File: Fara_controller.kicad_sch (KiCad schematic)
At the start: 74 parts, among them U1 XL1509-12, U2 XL1509-05, U3 TPS61165DBV, U4 TPS61165DBV, U6 TPS61165DBV, X1 Conn_01x02, X10 Conn_01x02, X11 Conn_01x02, X12 Conn_01x02, X13 Conn_01x02, X14 Conn_01x02, X18 Objective, X19 Conn_01x02, X2 Conn_01x02, X20 Conn_01x03, X21 Conn_01x03, X3 Conn_01x02, X4 Conn_01x02, X5 Fan_3pin, X6 Fan_3pin, X7 Fan_3pin, X8 Fan_3pin, X9 Conn_01x02

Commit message: v0.2 draft decomposition was made
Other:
- moved on the sheet: C15, C9, L5, R18, R19, R20, R21, R22, R23, R3, R7, R8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

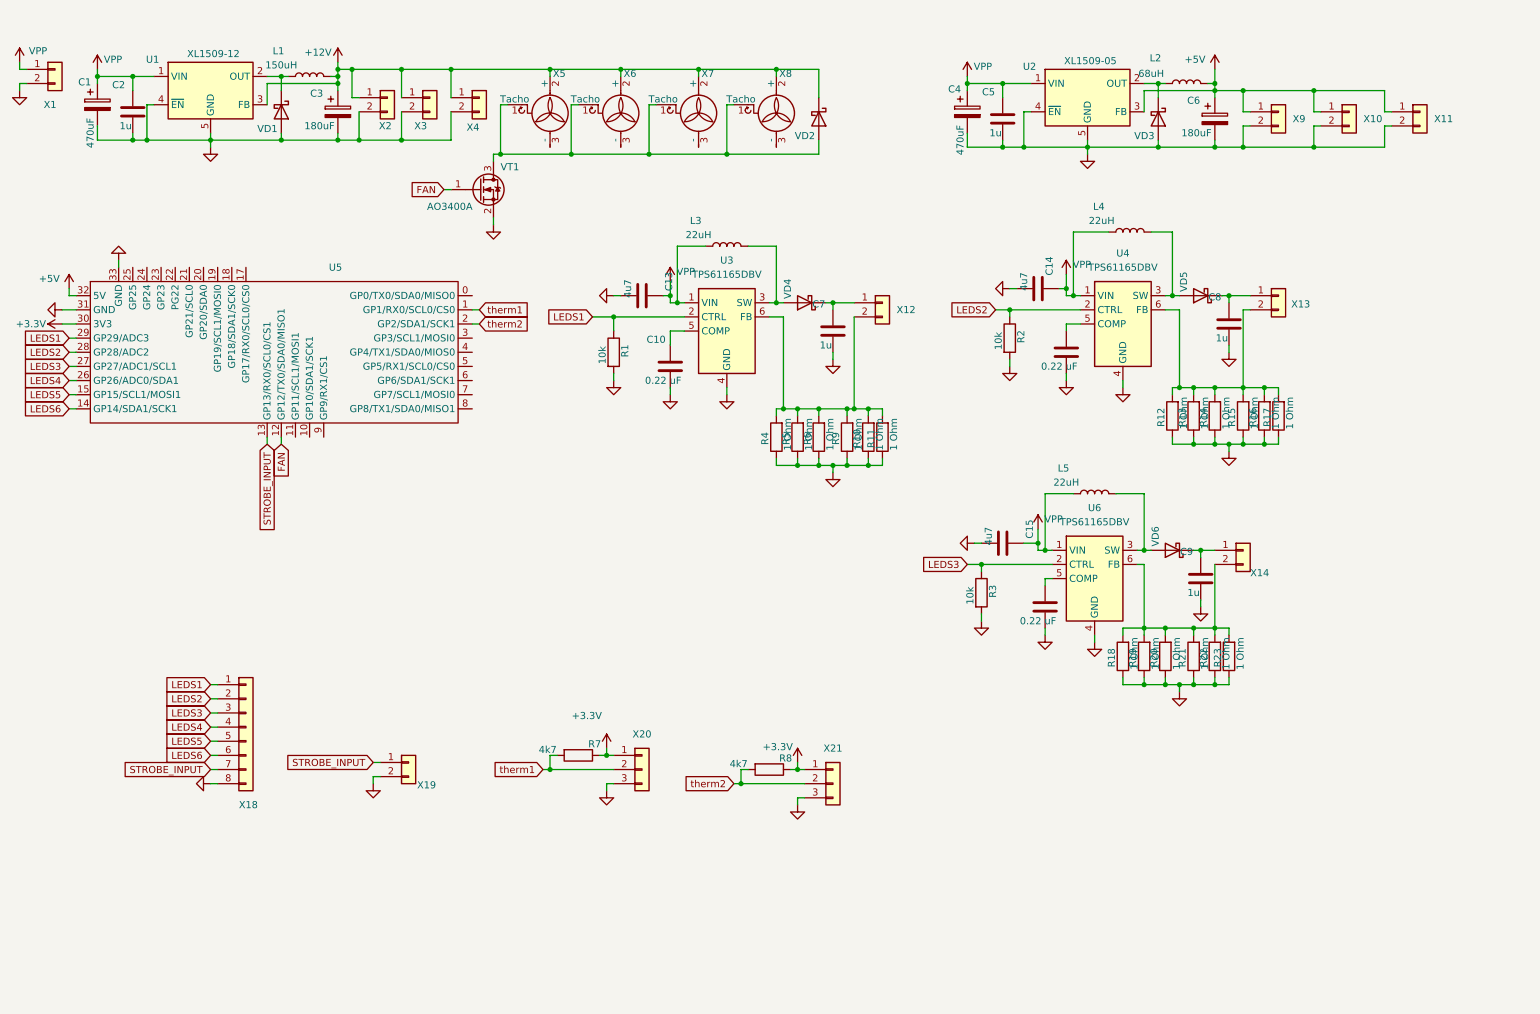
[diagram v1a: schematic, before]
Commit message: v0.3 4th driver was decomposed
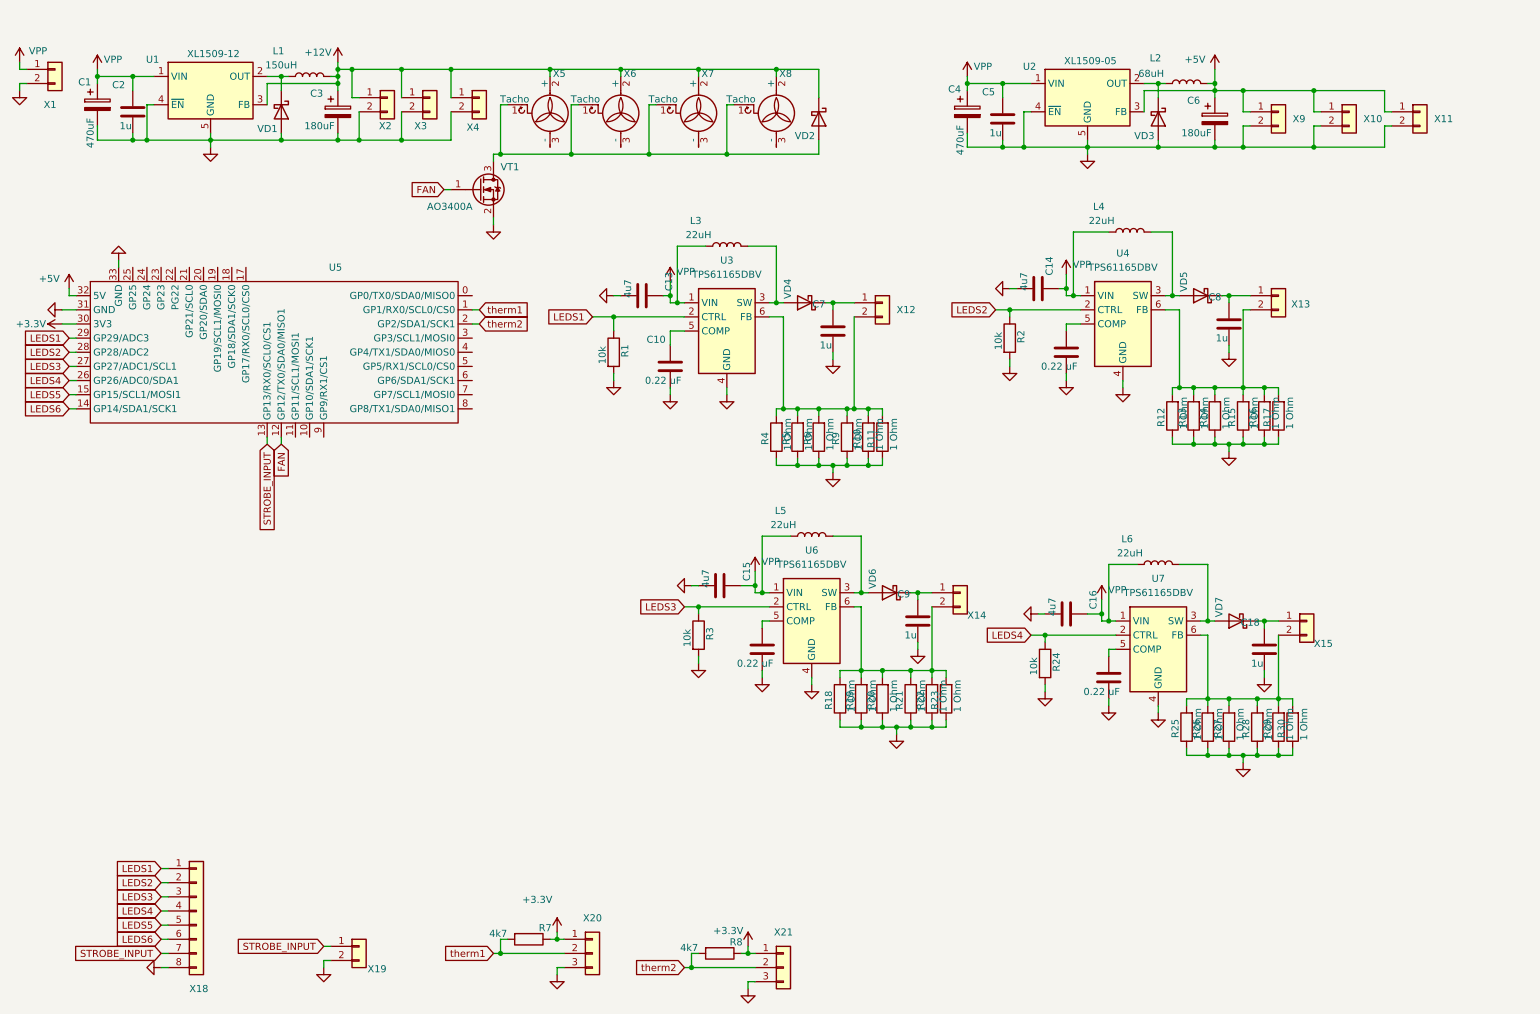
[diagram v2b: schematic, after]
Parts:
- added C16: 4u7, Capacitor_SMD:C_0805_2012Metric_Pad1.18x1.45mm_HandSolder, symbol Device:C
- added C17: 0.22 uF, Capacitor_SMD:C_0603_1608Metric_Pad1.08x0.95mm_HandSolder, symbol Device:C
- added C18: 1u, Capacitor_SMD:C_0603_1608Metric_Pad1.08x0.95mm_HandSolder, symbol Device:C
- added L6: 22uH, Inductor_SMD:L_7.3x7.3_H4.5, symbol Device:L
- added R24: 10k, Resistor_SMD:R_0603_1608Metric_Pad0.98x0.95mm_HandSolder, symbol Device:R
- added R25, R26, R27, R28, R29, R30: 1 Ohm, Resistor_SMD:R_0603_1608Metric_Pad0.98x0.95mm_HandSolder, symbol Device:R
- added U7: TPS61165DBV, Package_TO_SOT_SMD:SOT-23-6, symbol Driver_LED:TPS61165DBV
- added VD7: CDBA3100-HF, Diode_SMD:D_SOD-123, symbol Diode:CDBA3100-HF
- added X15: Conn_01x02, Connector_JST:JST_XH_B2B-XH-A_1x02_P2.50mm_Vertical, symbol Connector_Generic:Conn_01x02
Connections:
- net GND: now also C16.2, C17.2, C18.2, R24.2, R25.1, R26.1, R27.1, R28.1, R29.1, R30.1, U7.4 (GND)
- net LEDS4: now also R24.1, U7.2 (CTRL)
- net VPP: now also C16.1, L6.1, U7.1 (VIN)
- new net: C18.1, VD7.1 (K), X15.1 (Pin_1)
- new net: R25.2, R26.2, R27.2, R28.2, R29.2, R30.2, U7.6 (FB), X15.2 (Pin_2)
- new net: C17.1, U7.5 (COMP)
- new net: L6.2, U7.3 (SW), VD7.2 (A)
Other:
- moved on the sheet: C15, C9, L5, R18, R19, R20, R21, R22, R23, R3, R7, R8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

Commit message: v0.5 actual state
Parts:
- added X16: Conn_01x02, Connector_JST:JST_XH_B2B-XH-A_1x02_P2.50mm_Vertical, symbol Connector_Generic:Conn_01x02
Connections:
- net +12V: now also X16.2 (Pin_2)
- net VPP: now also X16.1 (Pin_1)
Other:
- moved on the sheet: C2
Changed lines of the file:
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@@
 	)
 	(junction
+		(at 33.02 24.13)
+		(diameter 0)
+		(color 0 0 0 0)
+	)
+	(junction
 		(at 135.89 22.86)
 		(diameter 0)
@@
 	)
 	(junction
-		(at 34.29 24.13)
+		(at 33.02 35.56)
 		(diameter 0)
 		(color 0 0 0 0)
@@
 	)
 	(junction
-		(at 34.29 35.56)
-		(diameter 0)
-		(color 0 0 0 0)
-	)
-	(junction
 		(at 153.67 93.98)
 		(diameter 0)
@@
 	(wire
 		(pts
-			(xy 27.94 24.13) (xy 34.29 24.13)
+			(xy 27.94 24.13) (xy 33.02 24.13)
 		)
 		(stroke
@@
 	(wire
 		(pts
-			(xy 34.29 24.13) (xy 34.29 26.67)
+			(xy 33.02 24.13) (xy 33.02 26.67)
 		)
 		(stroke
@@
 	(wire
 		(pts
+			(xy 35.56 19.05) (xy 41.91 19.05)
+		)
+		(stroke
+			(width 0)
+			(type default)
+		)
+	)
+	(wire
+		(pts
 			(xy 196.85 120.65) (xy 198.12 120.65)
 		)
@@
 	(wire
 		(pts
+			(xy 41.91 17.78) (xy 41.91 19.05)
+		)
+		(stroke
+			(width 0)
+			(type default)
+		)
+	)
+	(wire
+		(pts
 			(xy 259.08 33.02) (xy 259.08 36.83)
 		)
@@
 	(wire
 		(pts
+			(xy 33.02 24.13) (xy 38.1 24.13)
+		)
+		(stroke
+			(width 0)
+			(type default)
+		)
+	)
+	(wire
+		(pts
 			(xy 132.08 64.77) (xy 133.35 64.77)
 		)
@@
 	(wire
 		(pts
-			(xy 27.94 35.56) (xy 34.29 35.56)
+			(xy 27.94 35.56) (xy 33.02 35.56)
 		)
 		(stroke
@@
 	(wire
 		(pts
-			(xy 34.29 35.56) (xy 36.83 35.56)
-		)
-		(stroke
-			(width 0)
-			(type default)
-		)
-	)
-	(wire
-		(pts
 			(xy 68.58 180.34) (xy 69.85 180.34)
 		)
@@
 	(wire
 		(pts
+			(xy 33.02 35.56) (xy 36.83 35.56)
+		)
+		(stroke
+			(width 0)
+			(type default)
+		)
+	)
+	(wire
+		(pts
 			(xy 149.86 24.13) (xy 149.86 22.86)
 		)
@@
 	(wire
 		(pts
-			(xy 34.29 34.29) (xy 34.29 35.56)
+			(xy 33.02 34.29) (xy 33.02 35.56)
 		)
 		(stroke
@@
 	(wire
 		(pts
+			(xy 33.02 19.05) (xy 33.02 24.13)
+		)
+		(stroke
+			(width 0)
+			(type default)
+		)
+	)
+	(wire
+		(pts
 			(xy 228.6 80.01) (xy 233.68 80.01)
 		)
@@
 	(wire
 		(pts
-			(xy 34.29 24.13) (xy 38.1 24.13)
-		)
-		(stroke
-			(width 0)
-			(type default)
-		)
-	)
-	(wire
-		(pts
 			(xy 240.03 124.46) (xy 240.03 135.89)
 		)
@@
 	(symbol
 		(lib_id "Device:C")
-		(at 34.29 30.48 0)
+		(at 33.02 30.48 0)
 		(unit 1)
 		(exclude_from_sim no)
@@
 		(dnp no)
 		(property "Reference" "C2"
-			(at 31.75 25.654 0)
+			(at 30.48 25.654 0)
 			(effects
 				(font
@@
 		)
 		(property "Value" "1u"
-			(at 33.02 33.02 0)
+			(at 31.75 33.02 0)
 			(effects
 				(font
@@
 		)
 		(property "Footprint" "Capacitor_SMD:C_0603_1608Metric_Pad1.08x0.95mm_HandSolder"
-			(at 35.2552 34.29 0)
+			(at 33.9852 34.29 0)
 			(effects
 				(font
@@
 		)
 		(property "Datasheet" "~"
-			(at 34.29 30.48 0)
+			(at 33.02 30.48 0)
 			(effects
 				(font
@@
 		)
 		(property "Description" ""
-			(at 34.29 30.48 0)
+			(at 33.02 30.48 0)
 			(effects
 				(font
@@
 	)
 	(symbol
+		(lib_id "power:+12V")
+		(at 41.91 17.78 0)
+		(mirror y)
+		(unit 1)
+		(exclude_from_sim no)
+		(in_bom yes)
+		(on_board yes)
+		(dnp no)
+		(property "Reference" "#PWR048"
+			(at 41.91 21.59 0)
+			(effects
+				(font
+					(size 1.27 1.27)
+				)
+				(hide yes)
+			)
+		)
+		(property "Value" "+12V"
+			(at 45.466 16.256 0)
+			(effects
+				(font
+					(size 1.27 1.27)
+				)
+			)
+		)
+		(property "Footprint" ""
+			(at 41.91 17.78 0)
+			(effects
+				(font
+					(size 1.27 1.27)
+				)
+				(hide yes)
+			)
+		)
+		(property "Datasheet" ""
+			(at 41.91 17.78 0)
+			(effects
+				(font
+					(size 1.27 1.27)
+				)
+				(hide yes)
+			)
+		)
+		(property "Description" ""
+			(at 41.91 17.78 0)
+			(effects
+				(font
+					(size 1.27 1.27)
+				)
+				(hide yes)
+			)
+		)
+		(pin "1"
+		)
+		(instances
+			(project "Fara_controller"
+				(path "/094c26f9-240e-403d-a8eb-e8e5b0100c1e"
+					(reference "#PWR048")
+					(unit 1)
+				)
+			)
+		)
+	)
+	(symbol
 		(lib_id "Connector_Generic:Conn_01x02")
 		(at 245.11 121.92 0)
@@
 					(unit 1)
 				)
+			)
+		)
+	)
+	(symbol
+		(lib_id "Connector_Generic:Conn_01x02")
+		(at 33.02 13.97 90)
+		(unit 1)
+		(exclude_from_sim no)
+		(in_bom yes)
+		(on_board yes)
+		(dnp no)
+		(property "Reference" "X16"
+			(at 40.894 13.716 90)
+			(effects
+				(font
+					(size 1.27 1.27)
+				)
+				(justify left)
+			)
+		)
+		(property "Value" "Conn_01x02"
+			(at 35.5599 11.43 0)
+			(effects
+				(font
+					(size 1.27 1.27)
+				)
+				(justify left)
+				(hide yes)
+			)
+		)
+		(property "Footprint" "Connector_JST:JST_XH_B2B-XH-A_1x02_P2.50mm_Vertical"
+			(at 33.02 13.97 0)
+			(effects
+				(font
+					(size 1.27 1.27)
+				)
+				(hide yes)
+			)
+		)
+		(property "Datasheet" "~"
+			(at 33.02 13.97 0)
+			(effects
+				(font
+					(size 1.27 1.27)
+				)
+				(hide yes)
+			)
+		)
+		(property "Description" "Generic connector, single row, 01x02, script generated (kicad-library-utils/schlib/autogen/connector/)"
+			(at 33.02 13.97 0)
+			(effects
+				(font
+					(size 1.27 1.27)
+				)
+				(hide yes)
+			)
+		)
+		(pin "1"
+		)
+		(pin "2"
+		)
+		(instances
+			(project "Fara_controller"
+				(path "/094c26f9-240e-403d-a8eb-e8e5b0100c1e"
+					(reference "X16")
+					(unit 1)
+				)

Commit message: v0.7 small changes
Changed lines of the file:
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@@
 		(on_board yes)
 		(dnp no)
-		(fields_autoplaced yes)
 		(property "Reference" "U3"
 			(at 140.97 57.15 0)
@@
 		)
 		(property "Value" "TPS61165DBV"
-			(at 140.97 59.69 0)
+			(at 141.732 60.96 0)
 			(effects
 				(font

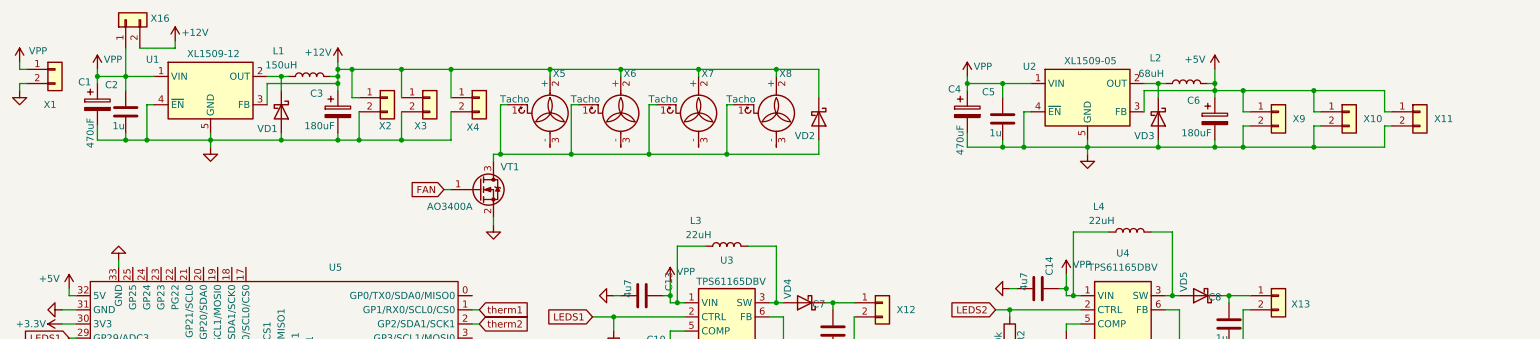
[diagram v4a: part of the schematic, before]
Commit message: v0.8 compact buck converters were added
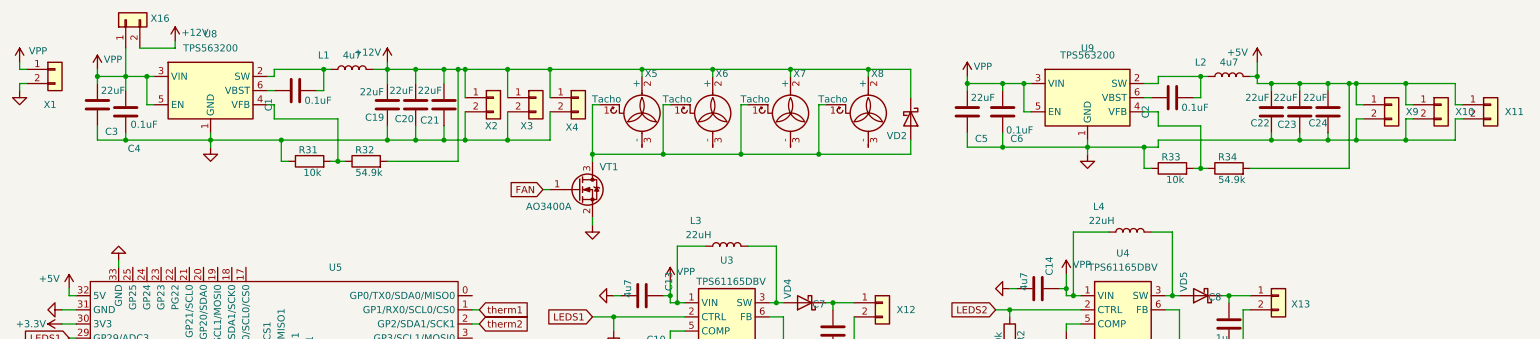
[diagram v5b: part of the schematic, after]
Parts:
- removed C1, C4: 470uF, Capacitor_THT:CP_Radial_D10.0mm_P5.00mm, symbol Device:C_Polarized
- removed C3, C6: 180uF, Capacitor_SMD:CP_Elec_6.3x7.7, symbol Device:C_Polarized
- removed U1: XL1509-12, Package_SO:SOIC-8-1EP_3.9x4.9mm_P1.27mm_EP2.95x4.9mm_Mask2.71x3.4mm_ThermalVias, symbol My_8_lib_sym:XL1509-3.3
- removed U2: XL1509-05, Package_SO:SOIC-8-1EP_3.9x4.9mm_P1.27mm_EP2.95x4.9mm_Mask2.71x3.4mm_ThermalVias, symbol My_8_lib_sym:XL1509-3.3
- removed VD1, VD3: CDBA3100-HF, Diode_SMD:D_SOD-123, symbol Diode:CDBA3100-HF
- added C1, C4, C6: 0.1uF, Capacitor_SMD:C_0603_1608Metric_Pad1.08x0.95mm_HandSolder, symbol Device:C
- added C19, C20, C21, C22, C23, C24, C3: 22uF, Capacitor_SMD:C_0805_2012Metric_Pad1.18x1.45mm_HandSolder, symbol Device:C
- added R31, R33: 10k, Resistor_SMD:R_0603_1608Metric_Pad0.98x0.95mm_HandSolder, symbol Device:R
- added R32, R34: 54.9k, Resistor_SMD:R_0603_1608Metric_Pad0.98x0.95mm_HandSolder, symbol Device:R
- added U8, U9: TPS563200, Package_TO_SOT_SMD:SOT-23-6, symbol Regulator_Switching:TPS563200
- C2: value 1u -> 0.1uF
- C5: value 1u -> 22uF; footprint Capacitor_SMD:C_0603_1608Metric_Pad1.08x0.95mm_HandSolder -> Capacitor_SMD:C_0805_2012Metric_Pad1.18x1.45mm_HandSolder
- L1: value 150uH -> 4u7; footprint Inductor_SMD:L_TDK_VLS6045EX_VLS6045AF -> Inductor_SMD:L_Chilisin_BMRx00040412
- L2: value 68uH -> 4u7; footprint Inductor_SMD:L_Bourns_SRP1050WA -> Inductor_SMD:L_Chilisin_BMRx00040412
- VD2: footprint Diode_SMD:D_SMA -> Diode_SMD:D_SOD-123
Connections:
- net +12V: now also C19.2, C20.2, C21.2, R32.2
- net +5V: now also C22.2, C23.2, C24.2, R34.2
- net GND: now also C5.1, C19.1, C20.1, C21.1, C22.1, C23.1, C24.1, C3.1, C4.1, C6.1, R31.1, R33.1, U8.1 (GND), U9.1 (GND); no longer C2.2, C5.2
- net VPP: now also C5.2, C3.2, C4.2, C6.2, U8.3 (VIN), U8.5 (EN), U9.3 (VIN), U9.5 (EN); no longer C2.1, C5.1
- net at L2.1: now also C2.2, U9.2 (SW)
- net at L1.1: now also C1.2, U8.2 (SW)
- new net: R33.2, R34.1, U9.4 (VFB)
- new net: R31.2, R32.1, U8.4 (VFB)
- new net: C1.1, U8.6 (VBST)
- new net: C2.1, U9.6 (VBST)
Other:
- moved on the sheet: VT1, X10, X11, X2, X3, X4, X5, X6, X7, X8, X9

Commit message: v0.9 small changes
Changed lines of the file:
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@@
 (kicad_sch
-	(version 20231120)
+	(version 20250114)
 	(generator "eeschema")
-	(generator_version "8.0")
+	(generator_version "9.0")
 	(paper "A4")
 	(junction
@@
 		)
 	)
+	(embedded_fonts no)
 )
